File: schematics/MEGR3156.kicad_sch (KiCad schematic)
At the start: 1 part

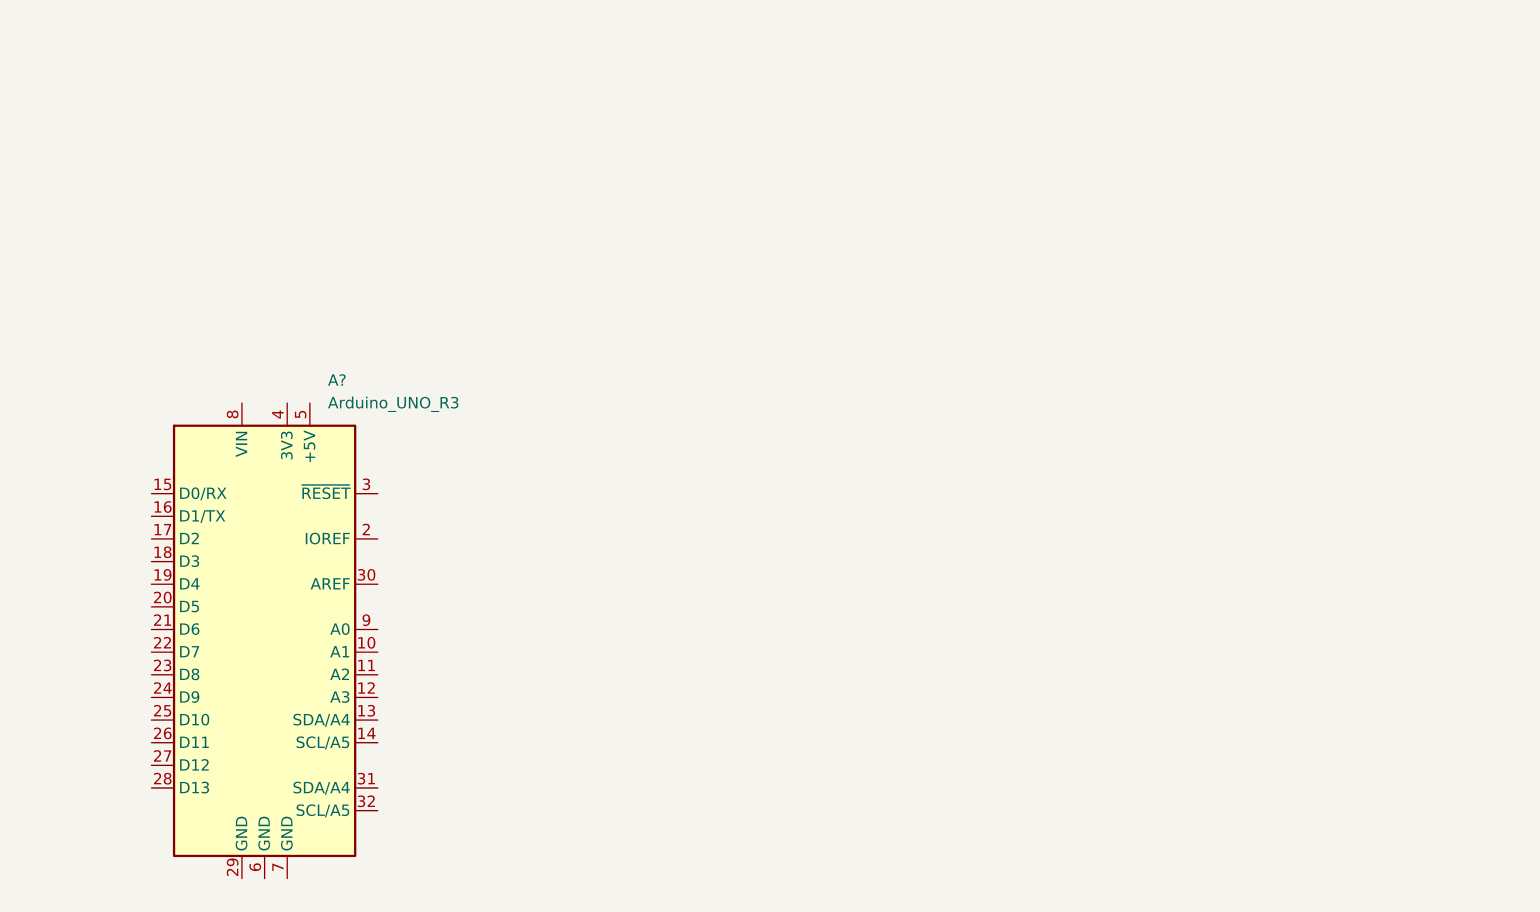
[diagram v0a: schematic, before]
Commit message: Progress
The joystick can now make a robot go forward and backwards
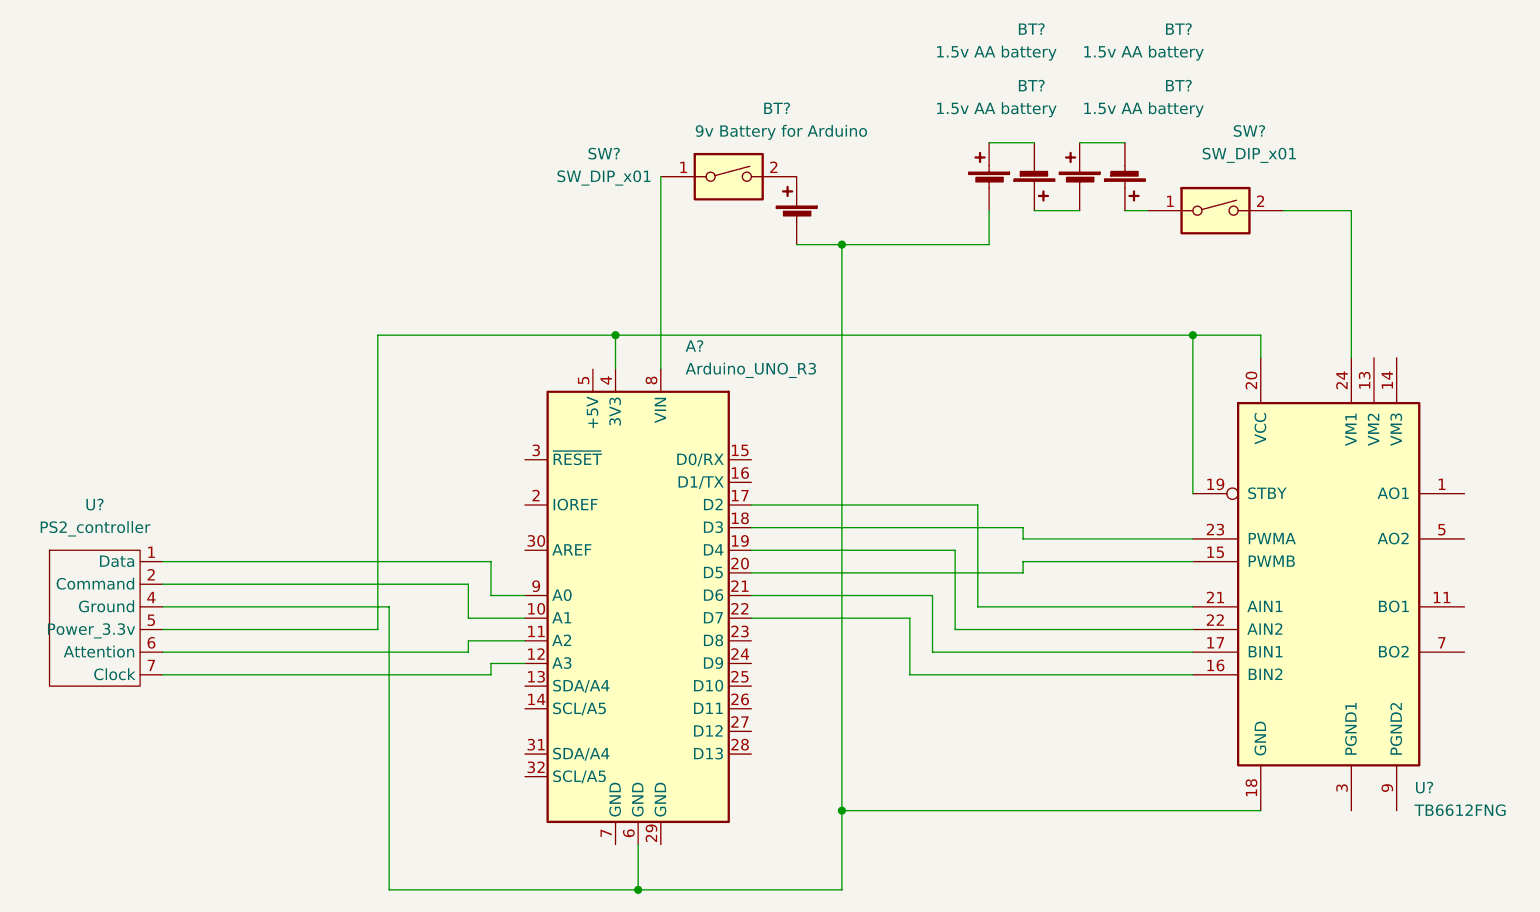
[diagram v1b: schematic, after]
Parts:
- added BT? (x4): 1.5v AA battery, symbol Device:Battery_Cell
- added BT?: 9v Battery for Arduino, symbol Device:Battery_Cell
- added SW? (x2): SW_DIP_x01, symbol Switch:SW_DIP_x01
- added U?: TB6612FNG, Package_SO:SSOP-24_5.3x8.2mm_P0.65mm, symbol Driver_Motor:TB6612FNG
- added U?: PS2_controller, symbol New_Library:PS2_controller
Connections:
- net at A?.10 (A1): now also U?.2 (Command)
- net at A?.11 (A2): now also U?.6 (Attention)
- net at A?.12 (A3): now also U?.7 (Clock)
- net at A?.17 (D2): now also U?.21 (AIN1)
- net at A?.18 (D3): now also U?.23 (PWMA)
- net at A?.19 (D4): now also U?.22 (AIN2)
- net at A?.20 (D5): now also U?.15 (PWMB)
- net at A?.21 (D6): now also U?.17 (BIN1)
- net at A?.22 (D7): now also U?.16 (BIN2)
- net at A?.4 (3V3): now also U?.19 (STBY), U?.20 (VCC), U?.5 (Power_3.3v)
- net at A?.6 (GND): now also BT?.2 (-), BT?.2 (-), U?.18 (GND), U?.4 (Ground)
- net at A?.8 (VIN): now also SW?.1
- net at A?.9 (A0): now also U?.1 (Data)
- new net: BT?.1 (+), SW?.1
- new net: SW?.2, U?.24 (VM1)
- new net: U?.1 (AO1), U?.2 (AO1)
- new net: U?.10 (PGND2), U?.9 (PGND2)
- new net: U?.11 (BO1), U?.12 (BO1)
- new net: U?.3 (PGND1), U?.4 (PGND1)
- new net: U?.5 (AO2), U?.6 (AO2)
- new net: U?.7 (BO2), U?.8 (BO2)
- new net: BT?.1 (+), BT?.2 (-) (x3)
- new net: BT?.1 (+), SW?.2
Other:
- moved on the sheet: A?
